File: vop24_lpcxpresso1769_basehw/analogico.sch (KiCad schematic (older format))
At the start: 13 parts, among them J201 Screw_Terminal_01x02, U201 LM358

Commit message: ESQ: modificaciones de etiquetas. Falta cambiar todas las conexiones de vcc
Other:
- moved on the sheet: C201, C202, J201, R201, R202, R203, R204, R205, R206, R207, R208, R209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

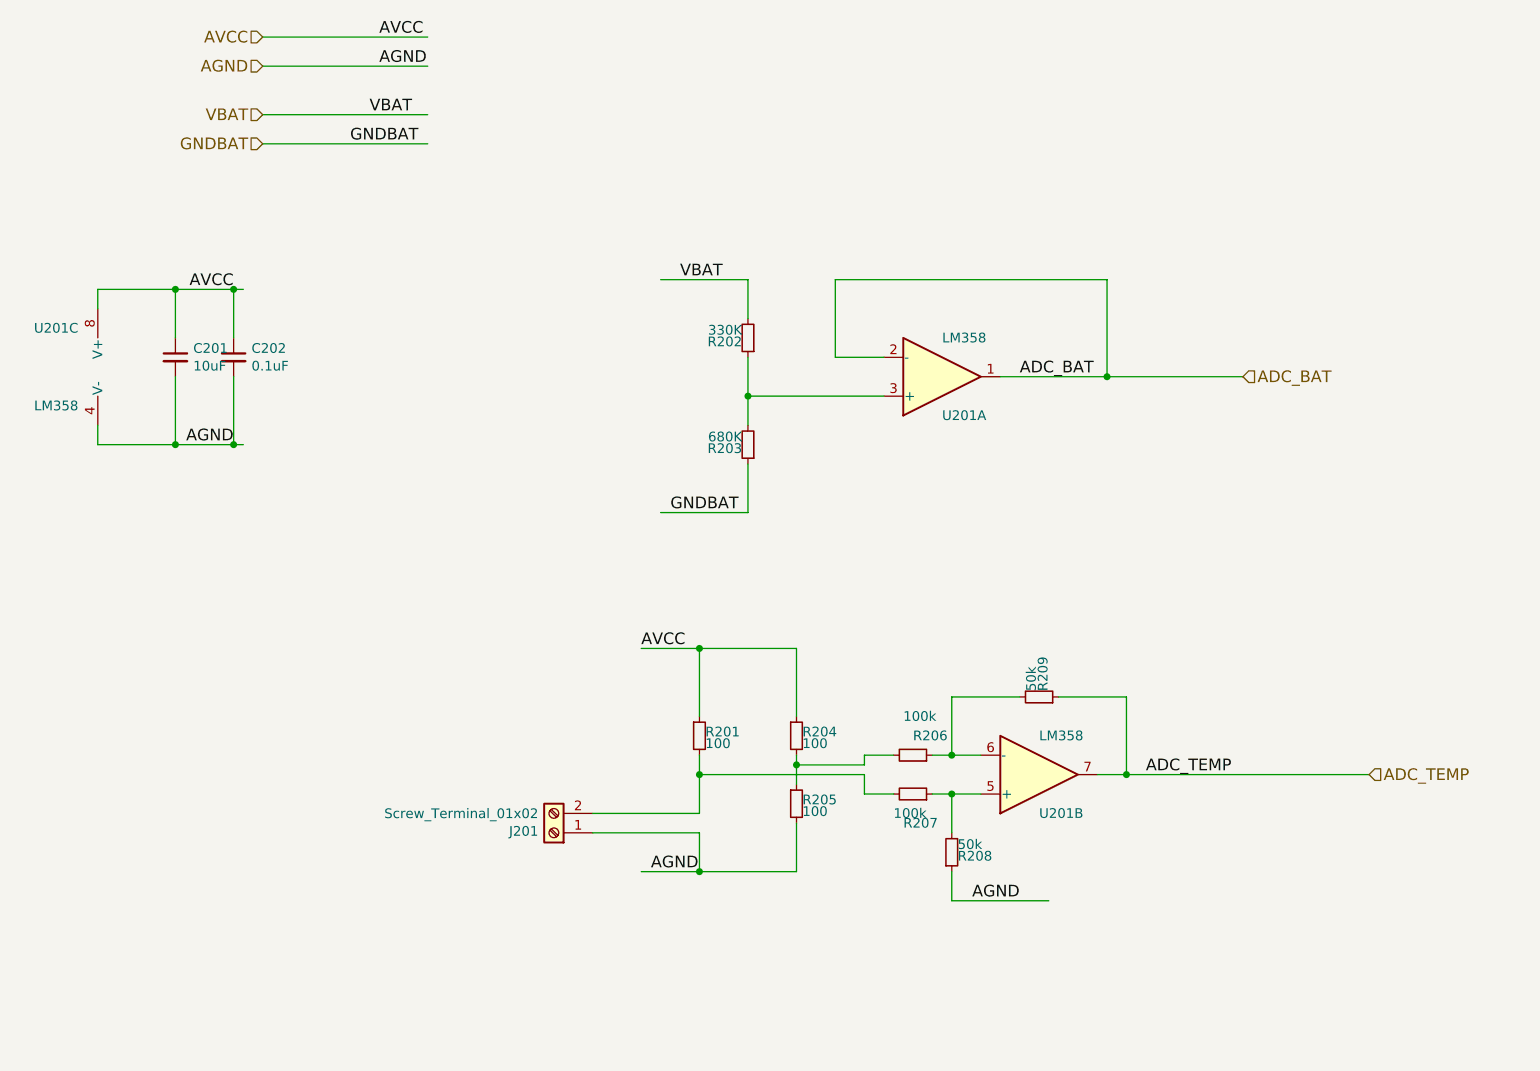
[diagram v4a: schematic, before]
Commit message: ESQ: todas las correcciones atendidas
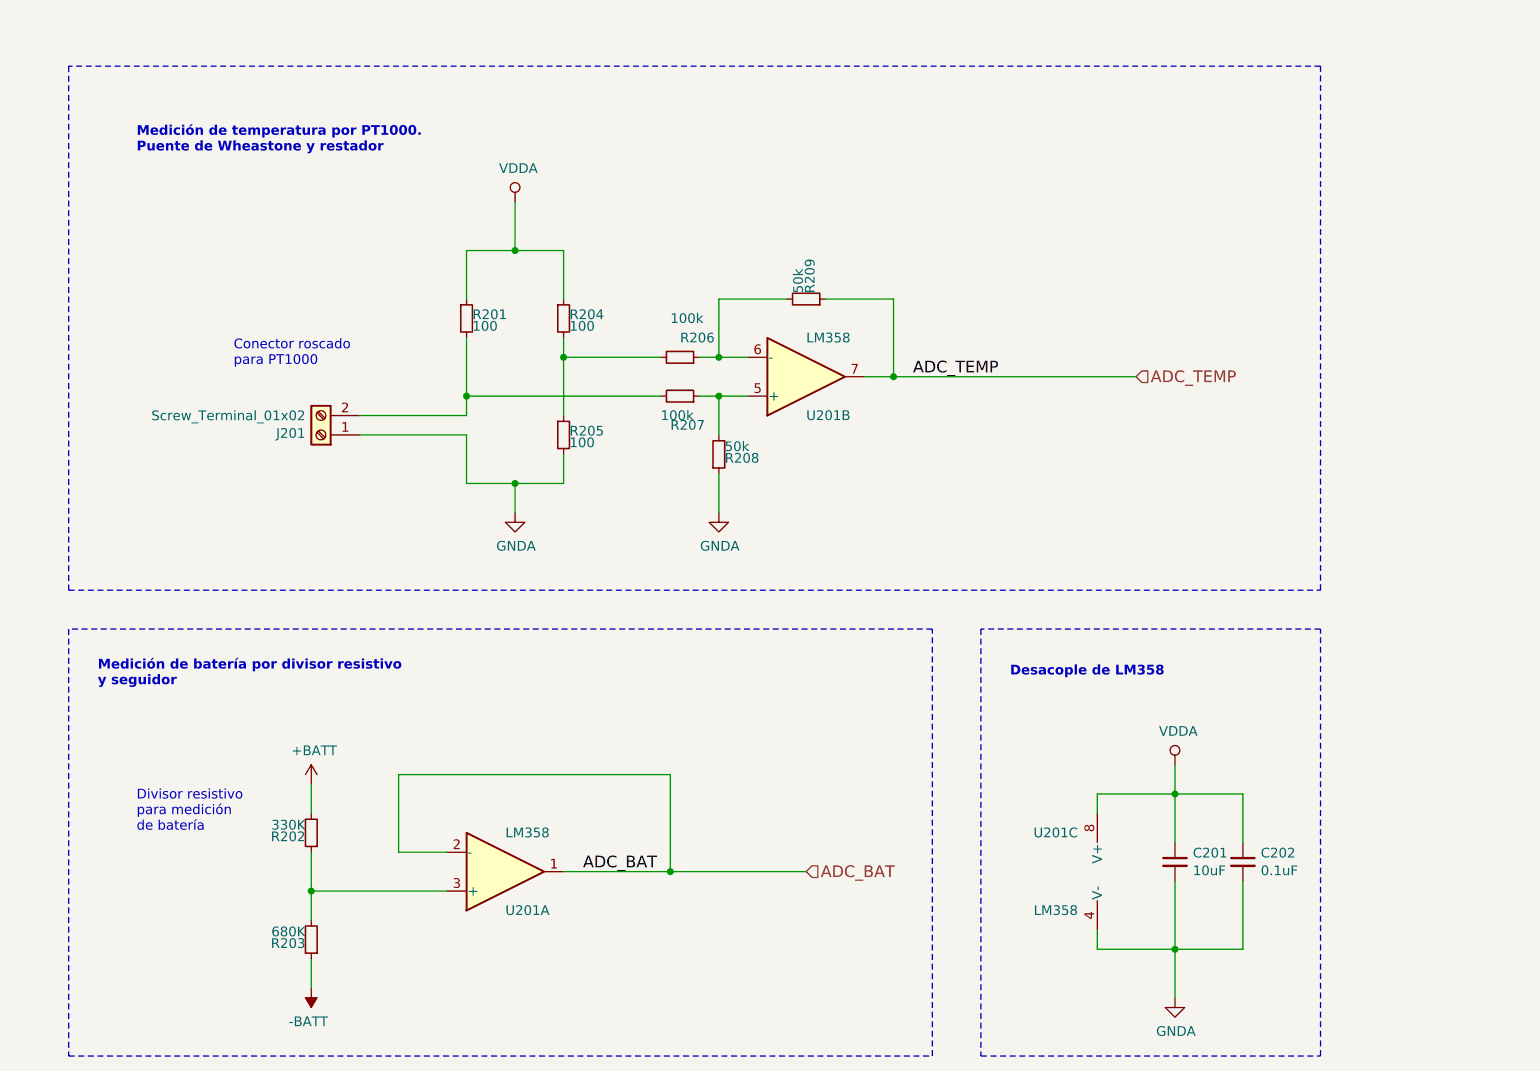
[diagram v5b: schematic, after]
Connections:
- net labels added: +BATT, -BATT, GNDA, VDDA
- net labels removed: AGND, AVCC, GNDBAT, VBAT
- wire segments 62 -> 53
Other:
- note added: "Conector roscado\npara PT1000"
- note added: "Desacople de LM358"
- note added: "Divisor resistivo\npara medición\nde batería"
- note added: "Medición de batería por divisor resistivo\ny seguidor"
- note added: "Medición de temperatura por PT1000. \nPuente de Wheastone y restador"
- moved on the sheet: C201, C202, J201, R201, R202, R203, R204, R205, R206, R207, R208, R209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
